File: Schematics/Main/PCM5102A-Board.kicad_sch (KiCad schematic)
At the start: 7 parts, among them U3 PCM5102A, U4 MIC5219-3.3YM5, U5 MIC5219-3.3YM5

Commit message: Added PCM5102A Board schematic
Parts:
- added C10, C2, C3, C4, C5, C7: 10 μF, symbol Device:C_Small
- added C11, C12, C13, C14: 2.2 μF, symbol Device:C_Small
- added C3, C6, C8, C9: 0.1 μF, symbol Device:C_Small
- added D1: LED, symbol Device:LED
- added J2: AudioJack3, symbol Connector_Audio:AudioJack3
- added JP1: SolderJumper_2_Open, symbol Jumper:SolderJumper_2_Open
- added R2, R3, R4, R5: 22 Ω, symbol Device:R
- added R6: 1 kΩ, symbol Device:R
- added R7, R8: 470 Ω, symbol Device:R
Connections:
- net BCK: now also R4.1; no longer U3.13 (BCK)
- net DIN: now also R3.1; no longer U3.14 (DIN)
- net GND: now also U3.19 (DGND), U3.20 (DVDD), U3.9 (AGND), U4.2 (GND), U5.2 (GND), U5.5 (OUT), C10.2, C13.1, C14.1, C2.2, C3.2, C3.2, C4.2, C5.1, C5.2, C6.1, C6.2, C7.1, C7.2, C8.1, C8.2, C9.2, D1.1 (K), J2.S, JP1.2 (B)
- net LRCK: now also R2.1; no longer U3.15 (LRCK)
- net SCK: now also R5.1; no longer U3.12 (SCK)
- net VDD: now also U4.1 (IN), U4.3 (EN), U5.1 (IN), U5.3 (EN), C3.1, C4.1
- net A3V3: now reaches U3.1 (CPVDD)
- net A3V3: now also U3.8 (AVDD), U4.5 (OUT), C2.1, C3.1, R6.1
- net at U3.18 (LDOO): now also C10.1, C9.1
- net at U3.2 (CAPP): now also C12.2
- net at U3.3 (CPGND): now also C11.1
- net at U3.4 (CAPM): now also C12.1
- net at U3.5 (VNEG): now also C11.2
- net at U3.6 (OUTL): now also R7.1
- net at U3.7 (OUTR): now also R8.1
- new net: R4.2, U3.13 (BCK)
- new net: JP1.1 (A), R2.2, U3.15 (LRCK)
- new net: D1.2 (A), R6.2
- new net: R5.2, U3.12 (SCK)
- new net: R3.2, U3.14 (DIN)
- new net LOUT: C14.2, J2.T, R7.2
- new net ROUT: C13.2, J2.R, R8.2
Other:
- moved on the sheet: JP2, JP3, JP4, JP5, U3, U4

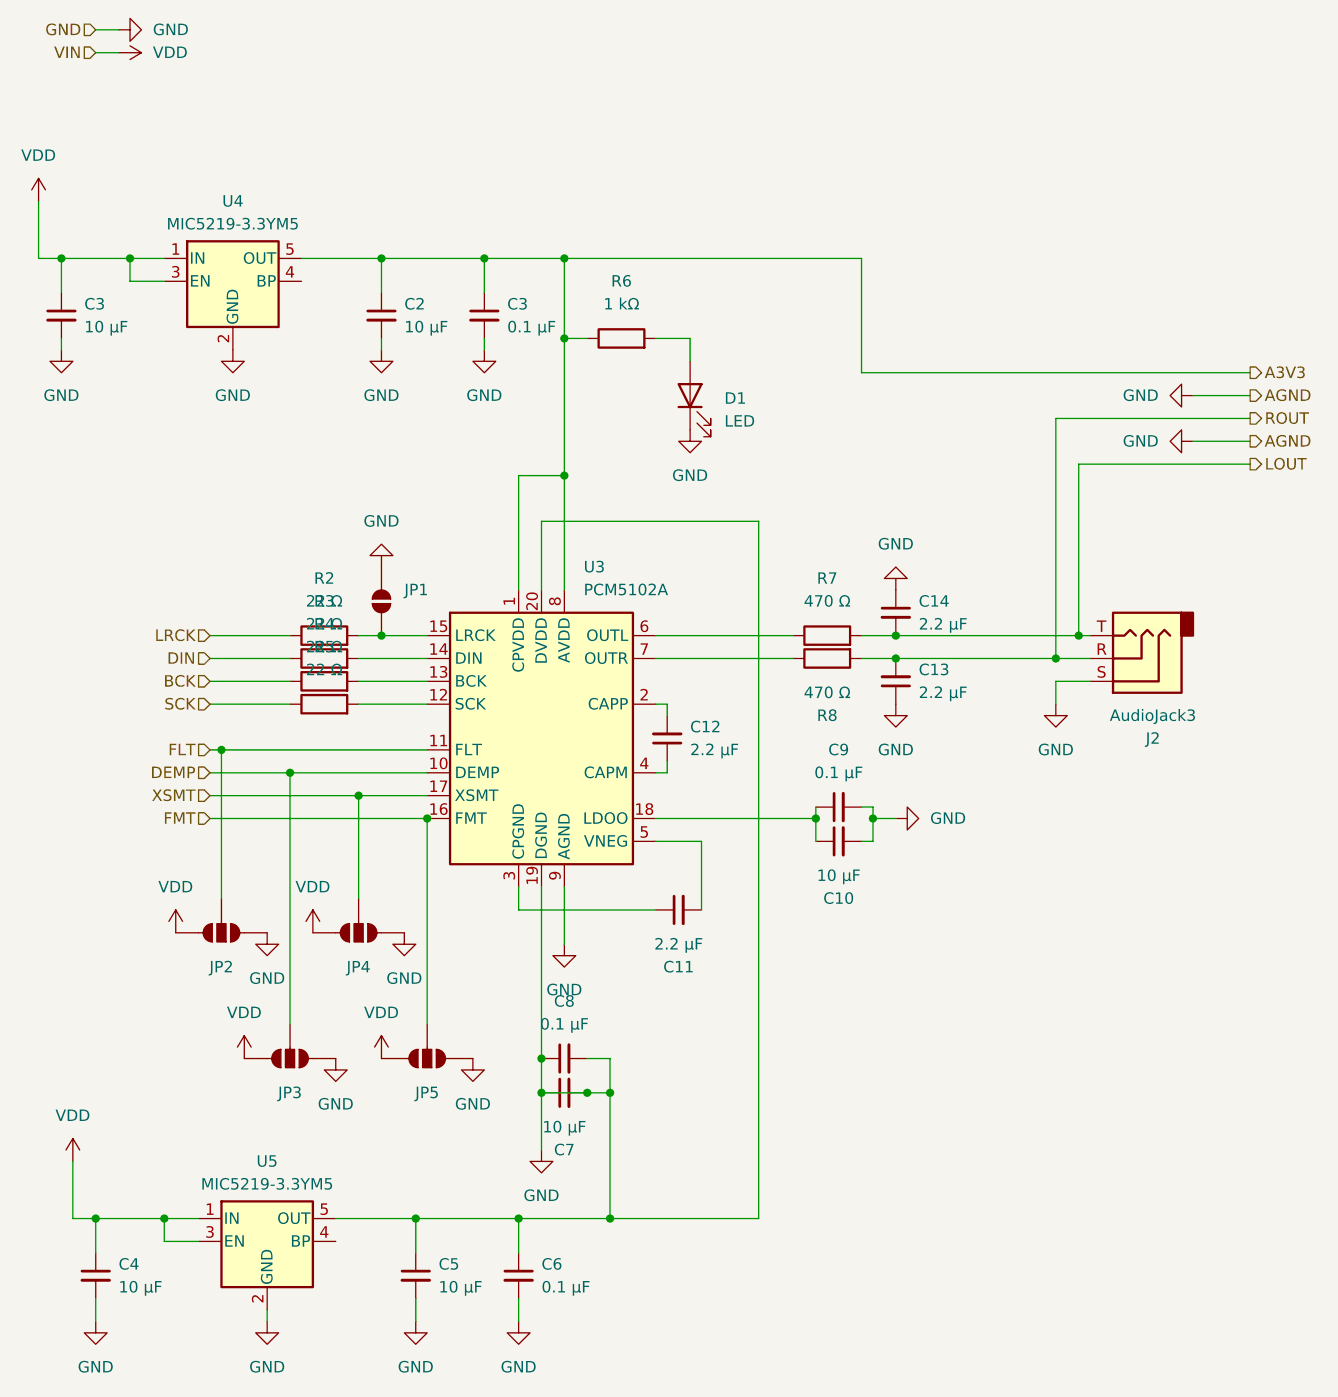
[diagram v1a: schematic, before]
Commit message: Added Audiosystem schematic
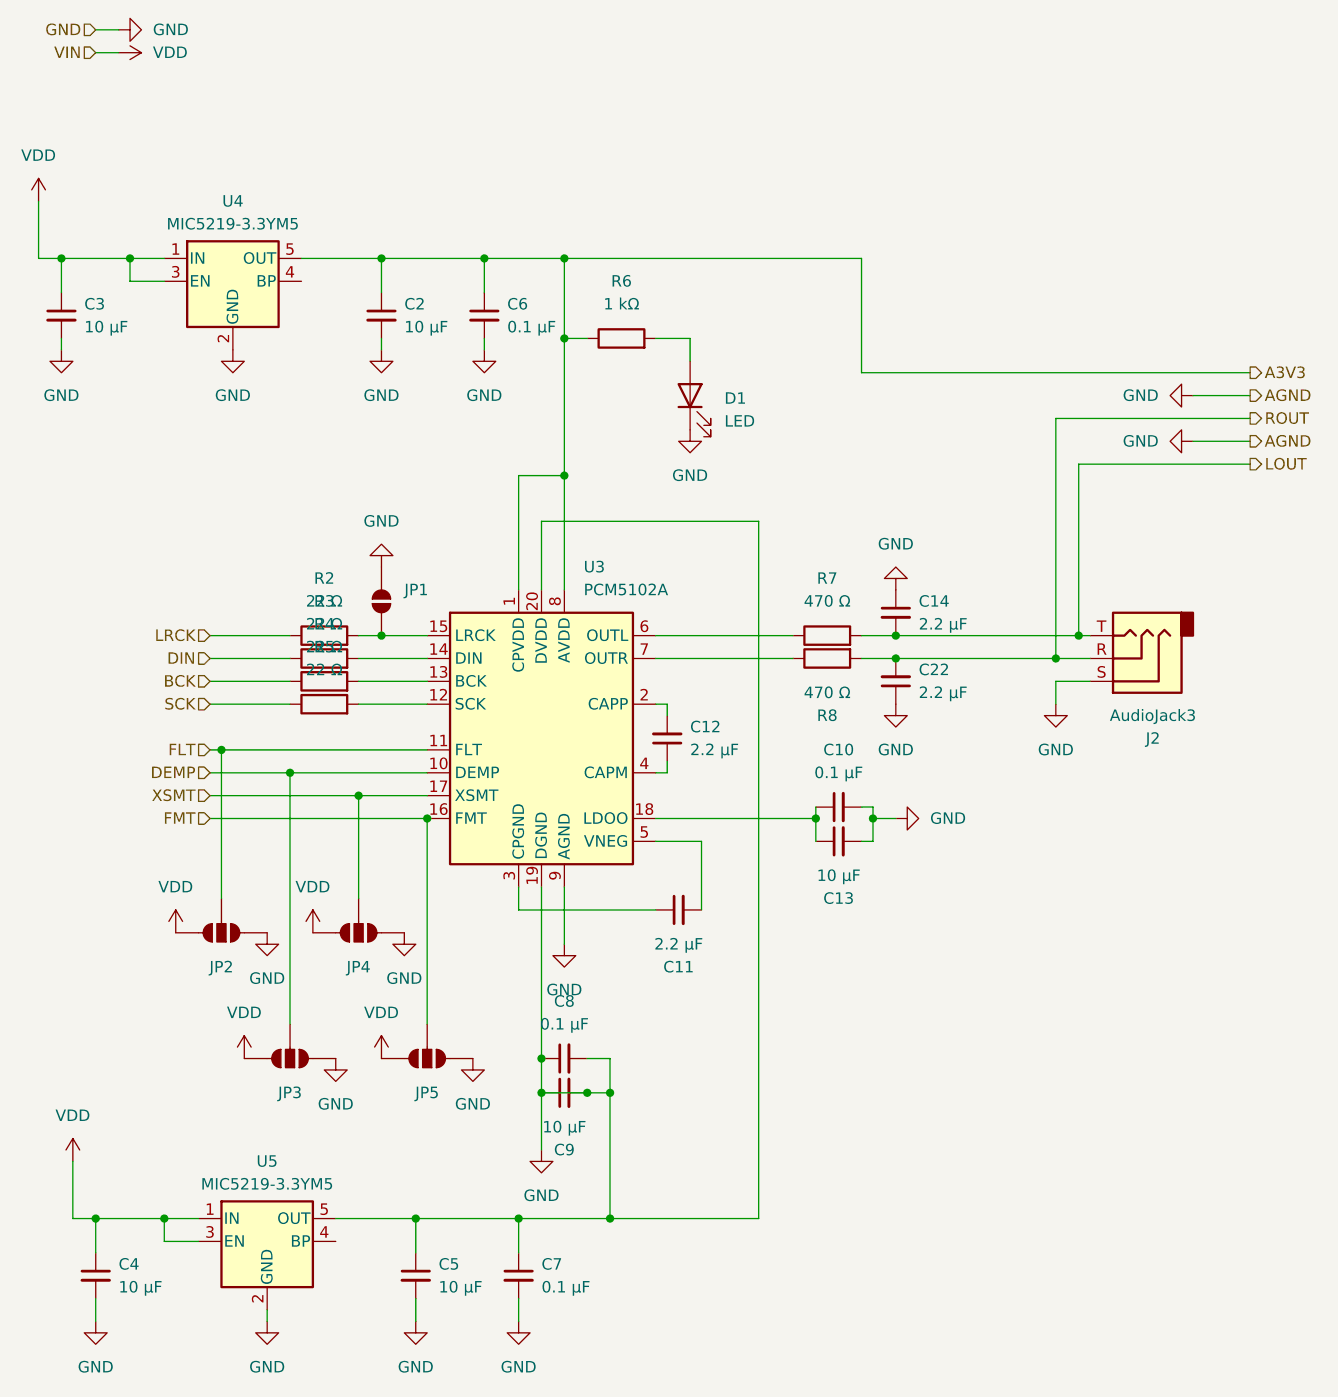
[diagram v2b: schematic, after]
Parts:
- renumbered C9 to C10, C10 to C13, C13 to C22, C3 to C6, C6 to C7, C7 to C9
